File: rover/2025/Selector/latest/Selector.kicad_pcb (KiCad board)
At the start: 2 copper layers, 51 x 47.5 mm, 17 parts, among them J2 JST4_Pin, J3 JST6_Pin, J4 JST3_Pin, J5 JST3_Pin, J6 JST2_Pin, U1 XT60PW-M

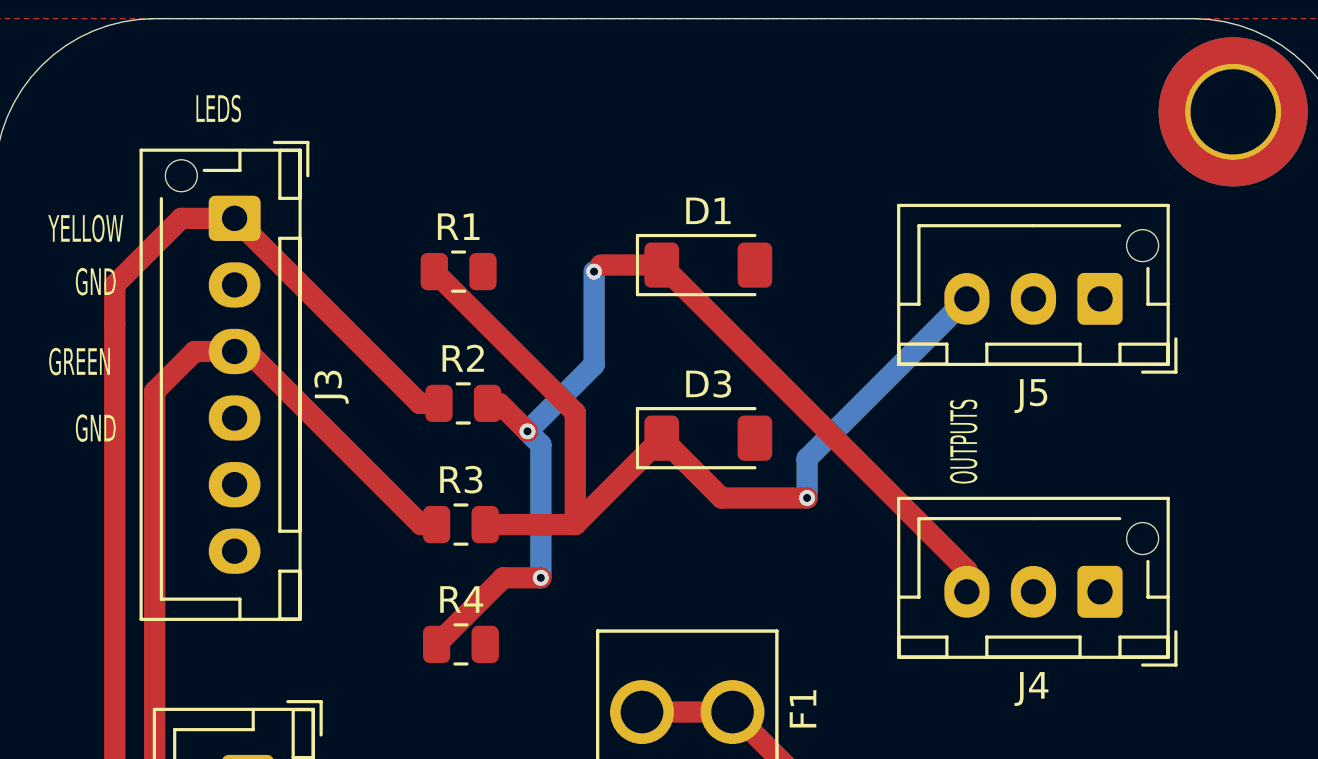
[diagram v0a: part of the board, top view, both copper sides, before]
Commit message: Selector PCB update footprints
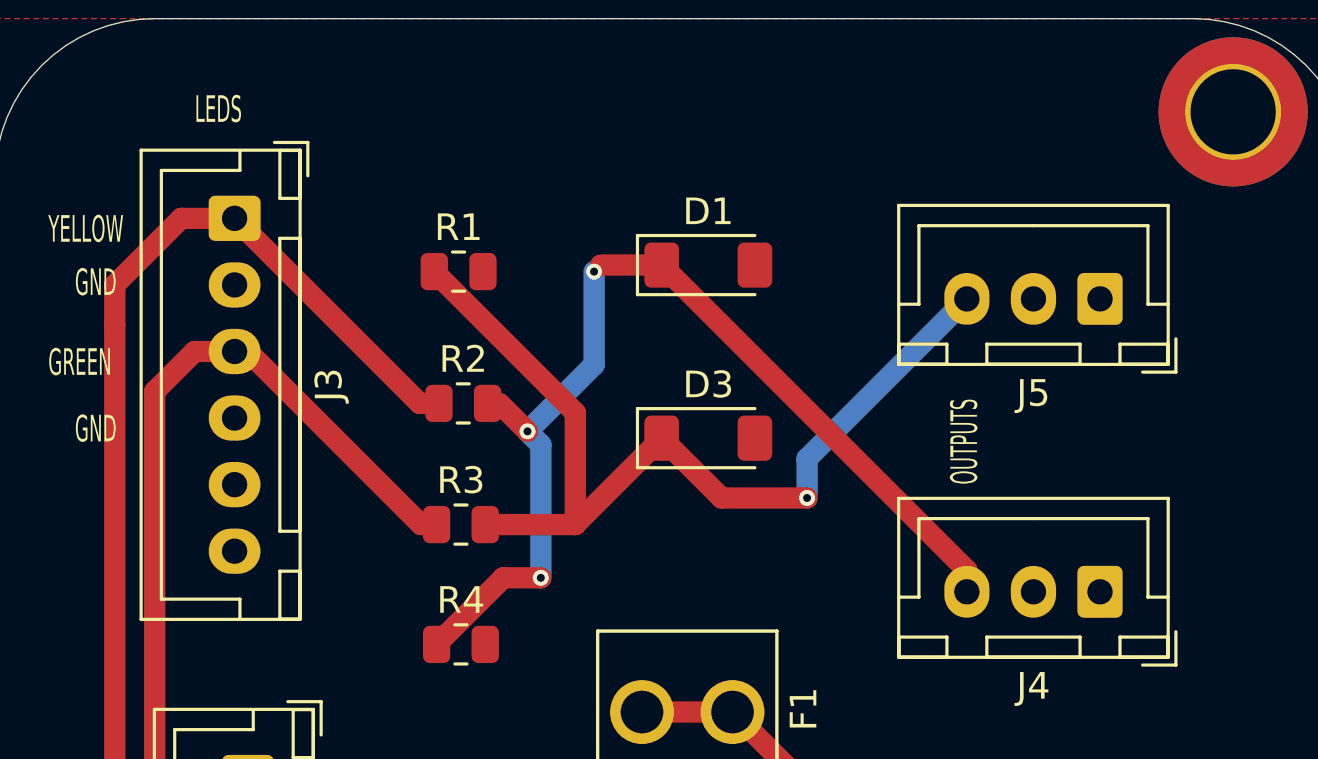
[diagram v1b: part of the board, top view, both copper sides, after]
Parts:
- J3: footprint Connector_JST:JST_XH_B6B-XH-AM_1x06_P2.50mm_Vertical -> Connector_JST:JST_XH_B6B-XH-A_1x06_P2.50mm_Vertical
- J4, J5: footprint Connector_JST:JST_XH_B3B-XH-AM_1x03_P2.50mm_Vertical -> Connector_JST:JST_XH_B3B-XH-A_1x03_P2.50mm_Vertical
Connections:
- F1 pad 1: Net-(U1-+) -> unconnected-(F1-Pad1)
- F1 pad 2: +24V -> unconnected-(F1-Pad2)
- U1 pad 2: Net-(U1-+) -> unconnected-(U1-+-Pad2)
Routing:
- net Net-(U1-+): track 16.9 -> 0.00 mm
- net (no net): track 0.00 -> 16.9 mm
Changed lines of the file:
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@@
 	(net 13 "Net-(D3-K)")
 	(net 14 "unconnected-(J2-Pad4)")
-	(net 15 "Net-(U1-+)")
+	(net 15 "unconnected-(F1-Pad1)")
 	(net 16 "Net-(J2-Pad1)")
+	(net 17 "unconnected-(F1-Pad2)")
+	(net 18 "unconnected-(U1-+-Pad2)")
 	(footprint "Connector_JST:JST_XH_B4B-XH-A_1x04_P2.50mm_Vertical"
 		(layer "F.Cu")
@@
 			)
 		)
+		(property "PACKAGE" "THT"
+			(at 0 0 -90)
+			(unlocked yes)
+			(layer "F.Fab")
+			(hide yes)
+			(effects
+				(font
+					(size 1 1)
+					(thickness 0.15)
+				)
+			)
+		)
 		(property ki_fp_filters "*Fuse*")
 		(sheetname "Root")
@@
 			(layers "*.Cu" "*.Mask")
 			(remove_unused_layers no)
-			(net 15 "Net-(U1-+)")
+			(net 15 "unconnected-(F1-Pad1)")
 			(pintype "power_out")
 			(solder_mask_margin 0.102)
@@
 			(layers "*.Cu" "*.Mask")
 			(remove_unused_layers no)
-			(net 15 "Net-(U1-+)")
+			(net 15 "unconnected-(F1-Pad1)")
 			(pintype "power_out")
 			(solder_mask_margin 0.102)
@@
 			(layers "*.Cu" "*.Mask")
 			(remove_unused_layers no)
-			(net 10 "+24V")
+			(net 17 "unconnected-(F1-Pad2)")
 			(pintype "power_in")
 			(solder_mask_margin 0.102)
@@
 			(layers "*.Cu" "*.Mask")
 			(remove_unused_layers no)
-			(net 10 "+24V")
+			(net 17 "unconnected-(F1-Pad2)")
 			(pintype "power_in")
 			(solder_mask_margin 0.102)
@@
 		)
 	)
-	(footprint "Connector_JST:JST_XH_B3B-XH-AM_1x03_P2.50mm_Vertical"
+	(footprint "Connector_JST:JST_XH_B3B-XH-A_1x03_P2.50mm_Vertical"
 		(layer "F.Cu")
 		(at 148.5 103.025 180)
-		(descr "JST XH series connector, B3B-XH-AM, with boss (http://www.jst-mfg.com/product/pdf/eng/eXH.pdf), generated with kicad-footprint-generator")
-		(tags "connector JST XH vertical boss")
+		(descr "JST XH series connector, B3B-XH-A (http://www.jst-mfg.com/product/pdf/eng/eXH.pdf), generated with kicad-footprint-generator")
+		(tags "connector JST XH vertical")
 		(property "Reference" "J4"
-			(at 2.5 -3.55 0)
+			(at 2.5 -3.55 180)
 			(layer "F.SilkS")
 			(effects
@@
 		)
 		(property "Value" "JST3_Pin"
-			(at 2.5 4.6 0)
+			(at 2.5 4.6 180)
 			(layer "F.Fab")
 			(effects
@@
 			)
 		)
-		(property "Footprint" "Connector_JST:JST_XH_B3B-XH-AM_1x03_P2.50mm_Vertical"
+		(property "Footprint" "Connector_JST:JST_XH_B3B-XH-A_1x03_P2.50mm_Vertical"
 			(at 0 0 180)
 			(unlocked yes)
@@
 				(font
 					(size 1.27 1.27)
-					(thickness 0.15)
 				)
 			)
@@
 				(font
 					(size 1.27 1.27)
-					(thickness 0.15)
 				)
 			)
@@
 				(font
 					(size 1.27 1.27)
-					(thickness 0.15)
 				)
 			)
@@
 		)
 		(fp_line
-			(start 2.5 2.75)
-			(end -0.74 2.75)
-			(stroke
-				(width 0.12)
-				(type solid)
-			)
-			(layer "F.SilkS")
-		)
-		(fp_line
 			(start 0.75 -1.7)
 			(end 4.25 -1.7)
@@
 		)
 		(fp_line
+			(start -1.8 2.75)
+			(end 2.5 2.75)
+			(stroke
+				(width 0.12)
+				(type solid)
+			)
+			(layer "F.SilkS")
+		)
+		(fp_line
 			(start -1.8 -0.2)
-			(end -1.8 1.14)
+			(end -1.8 2.75)
 			(stroke
 				(width 0.12)
@@
 		)
 		(fp_text user "${REFERENCE}"
-			(at 2.5 2.7 0)
+			(at 2.5 2.7 180)
 			(layer "F.Fab")
 			(effects
@@
 			)
 		)
-		(pad "" np_thru_hole circle
-			(at -1.6 2 180)
-			(size 1.2 1.2)
-			(drill 1.2)
-			(layers "*.Cu" "*.Mask")
-		)
 		(pad "1" thru_hole roundrect
 			(at 0 0 180)
@@
 			(pintype "passive")
 		)
-		(model "${KICAD8_3DMODEL_DIR}/Connector_JST.3dshapes/JST_XH_B3B-XH-AM_1x03_P2.50mm_Vertical.wrl"
+		(model "${KICAD8_3DMODEL_DIR}/Connector_JST.3dshapes/JST_XH_B3B-XH-A_1x03_P2.50mm_Vertical.wrl"
 			(offset
 				(xyz 0 0 0)
@@
 		)
 	)
-	(footprint "Connector_JST:JST_XH_B6B-XH-AM_1x06_P2.50mm_Vertical"
+	(footprint "Connector_JST:JST_XH_B6B-XH-A_1x06_P2.50mm_Vertical"
 		(layer "F.Cu")
 		(at 116 89 -90)
-		(descr "JST XH series connector, B6B-XH-AM, with boss (http://www.jst-mfg.com/product/pdf/eng/eXH.pdf), generated with kicad-footprint-generator")
-		(tags "connector JST XH vertical boss")
+		(descr "JST XH series connector, B6B-XH-A (http://www.jst-mfg.com/product/pdf/eng/eXH.pdf), generated with kicad-footprint-generator")
+		(tags "connector JST XH vertical")
 		(property "Reference" "J3"
-			(at 6.25 -3.55 90)
+			(at 6.25 -3.55 -90)
 			(layer "F.SilkS")
 			(effects
@@
 		)
 		(property "Value" "JST6_Pin"
-			(at 6.25 4.6 90)
+			(at 6.25 4.6 -90)
 			(layer "F.Fab")
 			(effects
@@
 			)
 		)
-		(property "Footprint" "Connector_JST:JST_XH_B6B-XH-AM_1x06_P2.50mm_Vertical"
+		(property "Footprint" "Connector_JST:JST_XH_B6B-XH-A_1x06_P2.50mm_Vertical"
 			(at 0 0 -90)
 			(unlocked yes)
@@
 				(font
 					(size 1.27 1.27)
-					(thickness 0.15)
 				)
 			)
@@
 				(font
 					(size 1.27 1.27)
-					(thickness 0.15)
 				)
 			)
@@
 				(font
 					(size 1.27 1.27)
-					(thickness 0.15)
 				)
 			)
@@
 		)
 		(fp_line
-			(start 6.25 2.75)
-			(end -0.74 2.75)
+			(start -1.8 2.75)
+			(end 6.25 2.75)
 			(stroke
 				(width 0.12)
@@
 		(fp_line
 			(start -1.8 -0.2)
-			(end -1.8 1.14)
+			(end -1.8 2.75)
 			(stroke
 				(width 0.12)
@@
 		)
 		(fp_text user "${REFERENCE}"
-			(at 6.25 2.7 90)
+			(at 6.25 2.7 -90)
 			(layer "F.Fab")
 			(effects
@@
 			)
 		)
-		(pad "" np_thru_hole circle
-			(at -1.6 2 270)
-			(size 1.2 1.2)
-			(drill 1.2)
-			(layers "*.Cu" "*.Mask")
-		)
 		(pad "1" thru_hole roundrect
 			(at 0 0 270)
@@
 			(pintype "passive")
 		)
-		(model "${KICAD8_3DMODEL_DIR}/Connector_JST.3dshapes/JST_XH_B6B-XH-AM_1x06_P2.50mm_Vertical.wrl"
+		(model "${KICAD8_3DMODEL_DIR}/Connector_JST.3dshapes/JST_XH_B6B-XH-A_1x06_P2.50mm_Vertical.wrl"
 			(offset
 				(xyz 0 0 0)
@@
 			(layers "*.Cu" "*.Mask")
 			(remove_unused_layers no)
-			(net 15 "Net-(U1-+)")
+			(net 18 "unconnected-(U1-+-Pad2)")
 			(pinfunction "+")
 			(pintype "power_out")
@@
 		(tags "resistor handsolder")
 		(property "Reference" "R5"
-			(at 0 -1.65 360)
+			(at 0 -1.65 0)
 			(layer "F.SilkS")
 			(effects
@@
 		)
 		(property "Value" "1K"
-			(at 0 1.65 360)
+			(at 0 1.65 0)
 			(layer "F.Fab")
 			(effects
@@
 		)
 		(fp_text user "${REFERENCE}"
-			(at 0 0 360)
+			(at 0 0 0)
 			(layer "F.Fab")
 			(effects
@@
 		)
 	)
-	(footprint "Connector_JST:JST_XH_B3B-XH-AM_1x03_P2.50mm_Vertical"
+	(footprint "Connector_JST:JST_XH_B3B-XH-A_1x03_P2.50mm_Vertical"
 		(layer "F.Cu")
 		(at 148.5 92.025 180)
-		(descr "JST XH series connector, B3B-XH-AM, with boss (http://www.jst-mfg.com/product/pdf/eng/eXH.pdf), generated with kicad-footprint-generator")
-		(tags "connector JST XH vertical boss")
+		(descr "JST XH series connector, B3B-XH-A (http://www.jst-mfg.com/product/pdf/eng/eXH.pdf), generated with kicad-footprint-generator")
+		(tags "connector JST XH vertical")
 		(property "Reference" "J5"
-			(at 2.5 -3.55 0)
+			(at 2.5 -3.55 180)
 			(layer "F.SilkS")
 			(effects
@@
 		)
 		(property "Value" "JST3_Pin"
-			(at 2.5 4.6 0)
+			(at 2.5 4.6 180)
 			(layer "F.Fab")
 			(effects
@@
 			)
 		)
-		(property "Footprint" "Connector_JST:JST_XH_B3B-XH-AM_1x03_P2.50mm_Vertical"
+		(property "Footprint" "Connector_JST:JST_XH_B3B-XH-A_1x03_P2.50mm_Vertical"
 			(at 0 0 180)
 			(unlocked yes)
@@
 				(font
 					(size 1.27 1.27)
-					(thickness 0.15)
 				)
 			)
@@
 				(font
 					(size 1.27 1.27)
-					(thickness 0.15)
 				)
 			)
@@
 				(font
 					(size 1.27 1.27)
-					(thickness 0.15)
 				)
 			)
@@
 		)
 		(fp_line
-			(start 2.5 2.75)
-			(end -0.74 2.75)
-			(stroke
-				(width 0.12)
-				(type solid)
-			)
-			(layer "F.SilkS")
-		)
-		(fp_line
 			(start 0.75 -1.7)
 			(end 4.25 -1.7)
@@
 		)
 		(fp_line
+			(start -1.8 2.75)
+			(end 2.5 2.75)
+			(stroke
+				(width 0.12)
+				(type solid)
+			)
+			(layer "F.SilkS")
+		)
+		(fp_line
 			(start -1.8 -0.2)
-			(end -1.8 1.14)
+			(end -1.8 2.75)
 			(stroke
 				(width 0.12)
@@
 		)
 		(fp_text user "${REFERENCE}"
-			(at 2.5 2.7 0)
+			(at 2.5 2.7 180)
 			(layer "F.Fab")
 			(effects
@@
 			)
 		)
-		(pad "" np_thru_hole circle
-			(at -1.6 2 180)
-			(size 1.2 1.2)
-			(drill 1.2)
-			(layers "*.Cu" "*.Mask")
-		)
 		(pad "1" thru_hole roundrect
 			(at 0 0 180)
@@
 			(pintype "passive")
 		)
-		(model "${KICAD8_3DMODEL_DIR}/Connector_JST.3dshapes/JST_XH_B3B-XH-AM_1x03_P2.50mm_Vertical.wrl"
+		(model "${KICAD8_3DMODEL_DIR}/Connector_JST.3dshapes/JST_XH_B3B-XH-A_1x03_P2.50mm_Vertical.wrl"
 			(offset
 				(xyz 0 0 0)
@@
 	)
 	(segment
+		(start 134.7 107.54)
+		(end 143.3 116.14)
+		(width 0.8)
+		(layer "F.Cu")
+		(net 0)
+	)
+	(segment
+		(start 143.3 116.14)
+		(end 143.3 117.45)
+		(width 0.8)
+		(layer "F.Cu")
+		(net 0)
+	)
+	(segment
+		(start 134.7 107.54)
+		(end 131.3 107.54)
+		(width 0.8)
+		(layer "F.Cu")
+		(net 0)
+	)
+	(segment
 		(start 129.5 91)
 		(end 129.745 90.755)
@@
 	)
 	(segment
-		(start 134.7 107.54)
-		(end 143.3 116.14)
-		(width 0.8)
-		(layer "F.Cu")
-		(net 15)
-	)
-	(segment
-		(start 143.3 116.14)
-		(end 143.3 117.45)
-		(width 0.8)
-		(layer "F.Cu")
-		(net 15)
-	)
-	(segment
-		(start 134.7 107.54)
-		(end 131.3 107.54)
-		(width 0.8)
-		(layer "F.Cu")
-		(net 15)
-	)
-	(segment

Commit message: Selector: Correction symboles
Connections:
- F1 pad 1: unconnected-(F1-Pad1) -> Net-(U1-+)
- F1 pad 2: unconnected-(F1-Pad2) -> +24V
- U1 pad 2: unconnected-(U1-+-Pad2) -> Net-(U1-+)
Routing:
- net Net-(U1-+): track 0.00 -> 16.9 mm
- net (no net): track 16.9 -> 0.00 mm
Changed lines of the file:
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@@
 	(net 13 "Net-(D3-K)")
 	(net 14 "unconnected-(J2-Pad4)")
-	(net 15 "unconnected-(F1-Pad1)")
+	(net 15 "Net-(U1-+)")
 	(net 16 "Net-(J2-Pad1)")
-	(net 17 "unconnected-(F1-Pad2)")
-	(net 18 "unconnected-(U1-+-Pad2)")
 	(footprint "Connector_JST:JST_XH_B4B-XH-A_1x04_P2.50mm_Vertical"
 		(layer "F.Cu")
@@
 			(layers "*.Cu" "*.Mask")
 			(remove_unused_layers no)
-			(net 15 "unconnected-(F1-Pad1)")
+			(net 15 "Net-(U1-+)")
 			(pintype "power_out")
 			(solder_mask_margin 0.102)
@@
 			(layers "*.Cu" "*.Mask")
 			(remove_unused_layers no)
-			(net 15 "unconnected-(F1-Pad1)")
+			(net 15 "Net-(U1-+)")
 			(pintype "power_out")
 			(solder_mask_margin 0.102)
@@
 			(layers "*.Cu" "*.Mask")
 			(remove_unused_layers no)
-			(net 17 "unconnected-(F1-Pad2)")
+			(net 10 "+24V")
 			(pintype "power_in")
 			(solder_mask_margin 0.102)
@@
 			(layers "*.Cu" "*.Mask")
 			(remove_unused_layers no)
-			(net 17 "unconnected-(F1-Pad2)")
+			(net 10 "+24V")
 			(pintype "power_in")
 			(solder_mask_margin 0.102)
@@
 			(layers "*.Cu" "*.Mask")
 			(remove_unused_layers no)
-			(net 18 "unconnected-(U1-+-Pad2)")
+			(net 15 "Net-(U1-+)")
 			(pinfunction "+")
 			(pintype "power_out")
@@
 	)
 	(segment
-		(start 134.7 107.54)
-		(end 143.3 116.14)
-		(width 0.8)
-		(layer "F.Cu")
-		(net 0)
-	)
-	(segment
-		(start 143.3 116.14)
-		(end 143.3 117.45)
-		(width 0.8)
-		(layer "F.Cu")
-		(net 0)
-	)
-	(segment
-		(start 134.7 107.54)
-		(end 131.3 107.54)
-		(width 0.8)
-		(layer "F.Cu")
-		(net 0)
-	)
-	(segment
 		(start 129.5 91)
 		(end 129.745 90.755)
@@
 	)
 	(segment
+		(start 134.7 107.54)
+		(end 143.3 116.14)
+		(width 0.8)
+		(layer "F.Cu")
+		(net 15)
+	)
+	(segment
+		(start 143.3 116.14)
+		(end 143.3 117.45)
+		(width 0.8)
+		(layer "F.Cu")
+		(net 15)
+	)
+	(segment
+		(start 134.7 107.54)
+		(end 131.3 107.54)
+		(width 0.8)
+		(layer "F.Cu")
+		(net 15)
+	)
+	(segment

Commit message: Selector Revision
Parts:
- added G***: LOGO, LOGO, B.Cu at (124.5, 89.0)
- moved R4 19.8 mm to (124.5, 85.2), turned to 180 degrees
- moved J4 11.0 mm to (148.5, 92.0)
- moved J5 11.0 mm to (148.5, 103.0)
- moved R2 6.95 mm to (124.5, 89.0)
- moved R1 6.50 mm to (124.5, 97.5), turned to 180 degrees
- moved R3 6.50 mm to (124.5, 94.0)
- moved D1 3.30 mm to (130.5, 91.0), turned to -90 degrees
- moved D3 3.02 mm to (136.2, 95.5), turned to 90 degrees
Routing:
- net Net-(D1-K): track 39.3 -> 22.5 mm, vias 3 -> 0
- net Net-(D3-K): track 36.0 -> 24.1 mm, vias 1 -> 0
- net POS1 & 2: track 43.4 -> 40.5 mm
- net POS2: track 33.5 -> 30.8 mm
- added copper zone on B.Cu, net GND
- added copper zone on In1.Cu, net GND
- added copper zone on In2.Cu, net GND
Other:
- copper layers 2 -> 4
- board text added: "${PROJECTNAME} REV${REVISION} by: ${AUTHOR} ${CURRENT_DATE} ${GROUP_NAME} ${TEAM}"

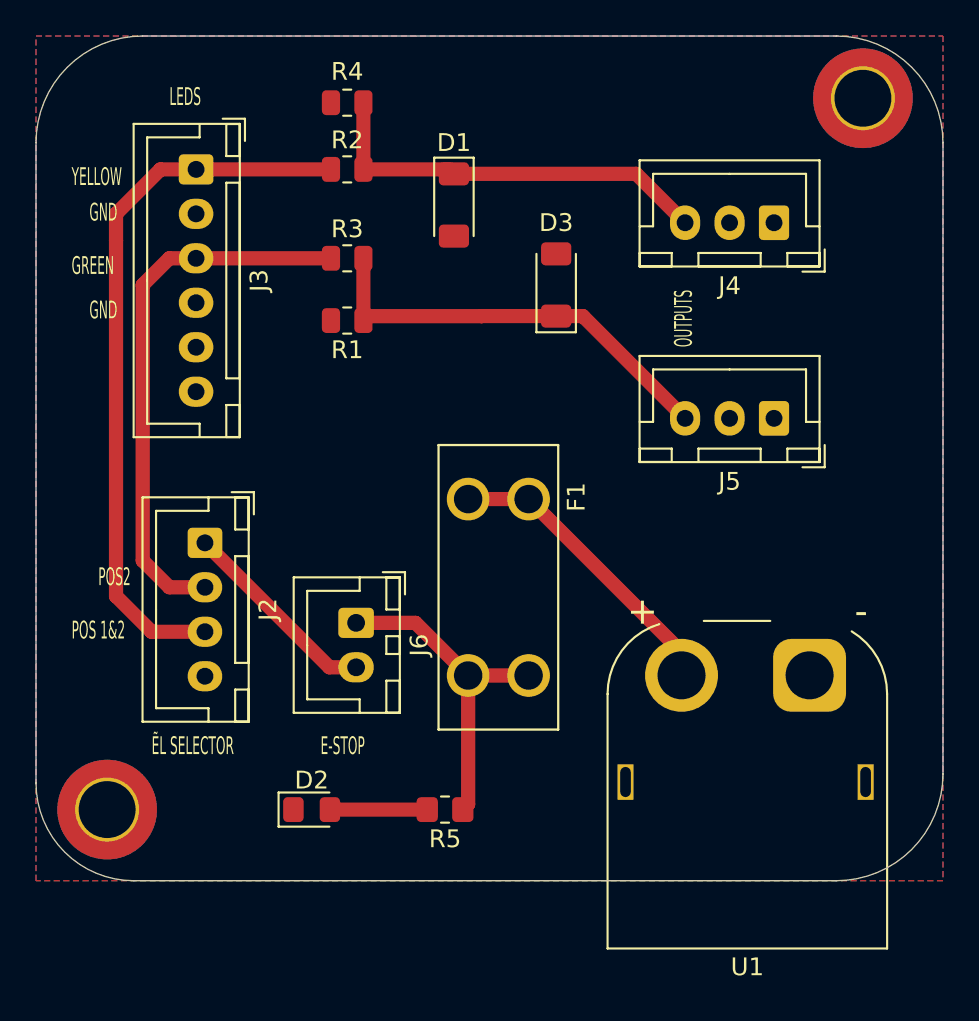
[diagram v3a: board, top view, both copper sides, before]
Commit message: Off board connections + silkscreen
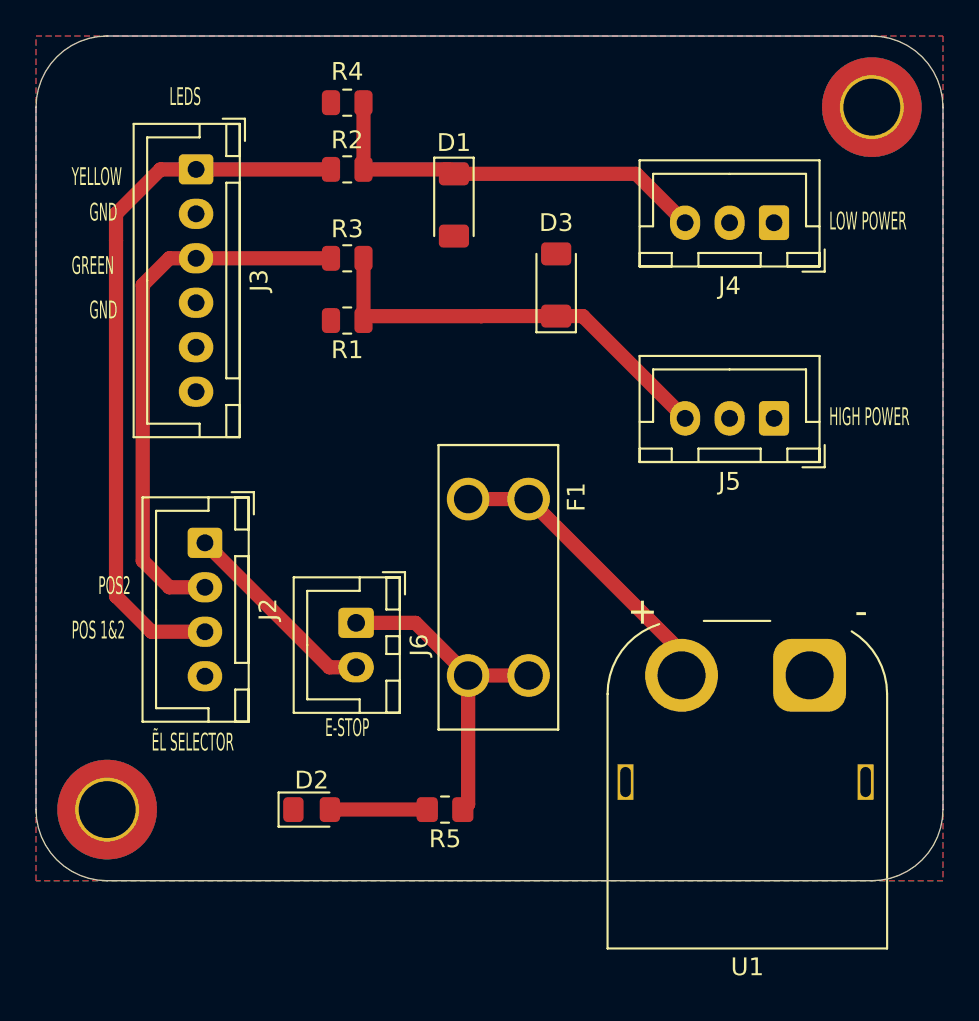
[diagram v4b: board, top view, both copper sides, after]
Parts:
- D2: value LED -> R
- moved H3 0.71 mm to (154.0, 85.5)
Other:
- outline, holes or cut-outs redrawn
- board text added: "HIGH POWER"
- board text added: "LOW POWER"
- board text removed: "OUTPUTS"
